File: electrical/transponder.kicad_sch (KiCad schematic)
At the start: 4 parts

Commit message: Updated with overview
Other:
- note added: "GDU45X"
- note added: "GPS175"
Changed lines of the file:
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@@
     (stroke (width 0) (type default))
+  )
+  (text "GDU45X" (at 114.3 147.32 0)
+    (effects (font (size 1.27 1.27)) (justify left bottom))
+  )
+  (text "GPS175" (at 114.3 157.48 0)
+    (effects (font (size 1.27 1.27)) (justify left bottom))
   )
   (hierarchical_label "ADSB_ETHERNET_OUT_1B" (shape output) (at 86.36 156.21 0) (fields_autoplaced)

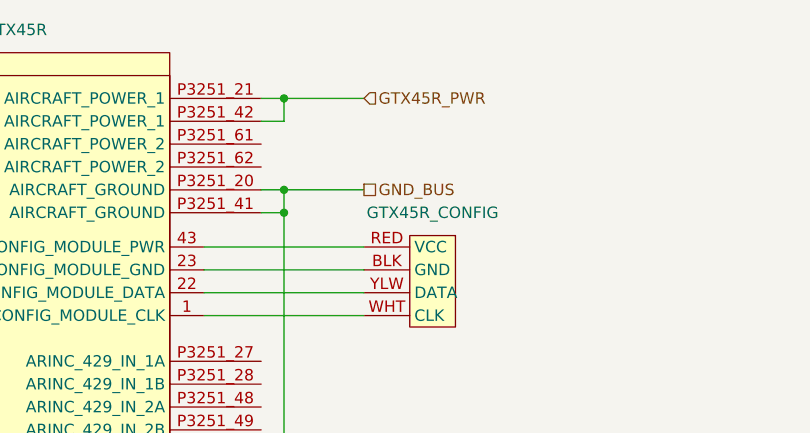
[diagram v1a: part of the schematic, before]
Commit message: Updated system overview and added Power 2 to GTX 45R.
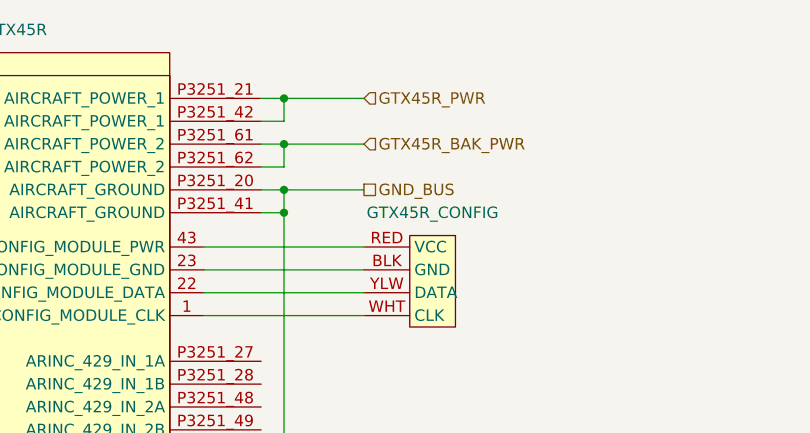
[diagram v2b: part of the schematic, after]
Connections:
- net GTX45R_BAK_PWR: now reaches GTX45R.P3251_61 (AIRCRAFT_POWER_2)
- net GTX45R_BAK_PWR: now also GTX45R.P3251_62 (AIRCRAFT_POWER_2)
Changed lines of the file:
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@@
   (junction (at 80.01 121.92) (diameter 0) (color 0 0 0 0)
+  )
+  (junction (at 80.01 41.91) (diameter 0) (color 0 0 0 0)
   )
   (junction (at 80.01 46.99) (diameter 0) (color 0 0 0 0)
@@
     (stroke (width 0) (type default))
   )
+  (wire (pts (xy 77.47 44.45) (xy 80.01 44.45))
+    (stroke (width 0) (type default))
+  )
   (wire (pts (xy 77.47 132.08) (xy 130.81 132.08))
     (stroke (width 0) (type default))
@@
     (stroke (width 0) (type default))
   )
+  (wire (pts (xy 80.01 44.45) (xy 80.01 41.91))
+    (stroke (width 0) (type default))
+  )
   (wire (pts (xy 128.27 127) (xy 128.27 134.62))
     (stroke (width 0) (type default))
@@
     (stroke (width 0) (type default))
   )
+  (wire (pts (xy 80.01 41.91) (xy 88.9 41.91))
+    (stroke (width 0) (type default))
+  )
   (wire (pts (xy 77.47 121.92) (xy 80.01 121.92))
+    (stroke (width 0) (type default))
+  )
+  (wire (pts (xy 77.47 41.91) (xy 80.01 41.91))
     (stroke (width 0) (type default))
   )
@@
     (effects (font (size 1.27 1.27)) (justify left))
   )
+  (hierarchical_label "GTX45R_BAK_PWR" (shape input) (at 88.9 41.91 0) (fields_autoplaced)
+    (effects (font (size 1.27 1.27)) (justify left))
+  )

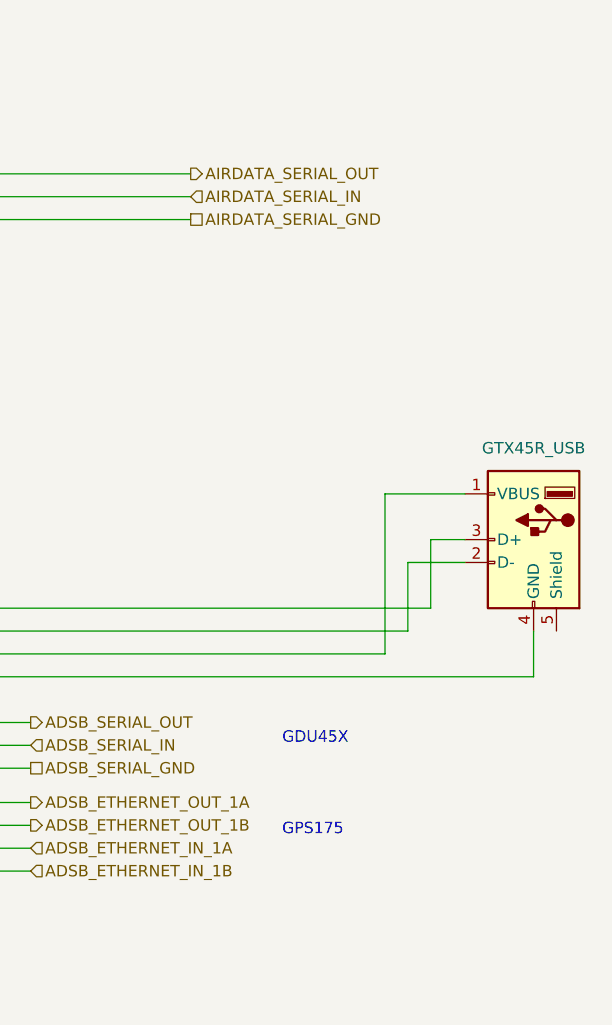
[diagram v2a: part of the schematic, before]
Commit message: Updated settings for RS-232, etc.
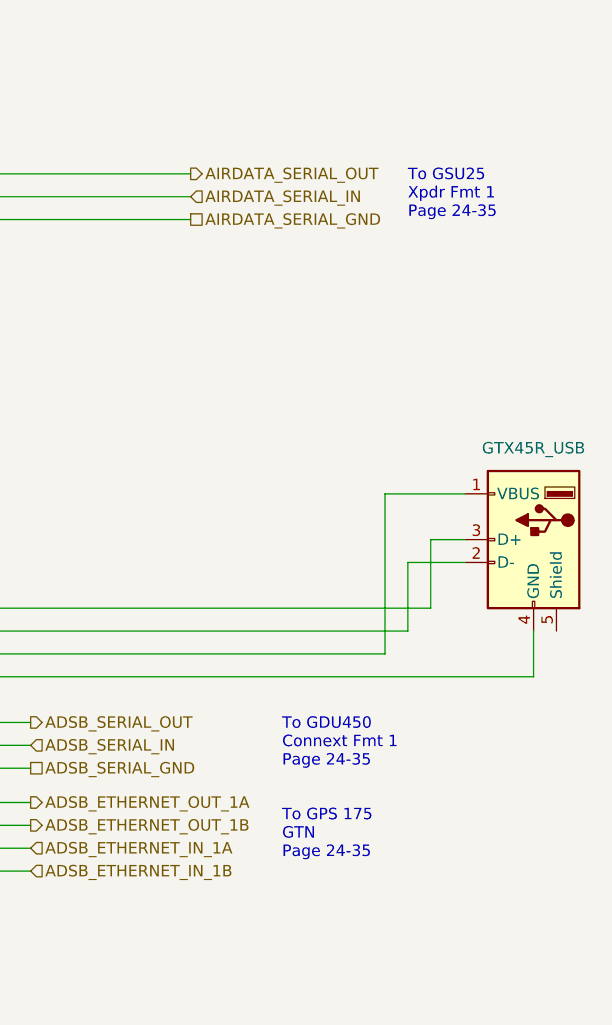
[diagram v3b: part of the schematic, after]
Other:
- note added: "To GDU450 Connext Fmt 1 Page 24-35"
- note added: "To GPS 175 GTN Page 24-35"
- note added: "To GSU25 Xpdr Fmt 1 Page 24-35"
- note removed: "GDU45X"
- note removed: "GPS175"
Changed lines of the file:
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@@
     (stroke (width 0) (type default))
   )
-  (text "GDU45X" (at 114.3 147.32 0)
+  (text "To GDU450\nConnext Fmt 1\nPage 24-35" (at 114.3 149.86 0)
     (effects (font (size 1.27 1.27)) (justify left bottom))
   )
-  (text "GPS175" (at 114.3 157.48 0)
+  (text "To GPS 175\nGTN\nPage 24-35" (at 114.3 160.02 0)
     (effects (font (size 1.27 1.27)) (justify left bottom))
   )
+  (text "To GSU25\nXpdr Fmt 1\nPage 24-35" (at 128.27 88.9 0)
+    (effects (font (size 1.27 1.27)) (justify left bottom))
+  )
